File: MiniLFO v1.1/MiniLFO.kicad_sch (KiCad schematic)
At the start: 18 parts, among them U1 TL074

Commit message: Updated docs
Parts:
- removed RANGE_SW1: SW_DPDT_x2, benjiaomodular:ToggleSwitch_MTS-202_DPDT, symbol Switch:SW_DPDT_x2
- added RANGE_SW1: SW_SPDT, benjiaomodular:ToggleSwitch_MTS-102_SPDT, symbol Switch:SW_SPDT
- C1: footprint Capacitor_SMD:C_0805_2012Metric_Pad1.18x1.45mm_HandSolder -> benjiaomodular:Capacitor_Radial_D5.0mm_P2.5mm
- C2: footprint Capacitor_SMD:C_0805_2012Metric_Pad1.18x1.45mm_HandSolder -> benjiaomodular:Capacitor_Rect_L7.2mm_W2.5mm_P5.00mm
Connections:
- net TRI: now also RANGE_SW1.2 (B)
- net at C1.2: now also RANGE_SW1.1 (A)
- net at C2.2: now also RANGE_SW1.3 (C)
- net SQR: no longer names the net of R5.1, U1.7
- no-connect marks 2 -> 1
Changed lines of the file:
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@@
   (title_block
     (title "MiniLFO")
-    (rev "v1.0")
+    (rev "v1.1")
   )
   (junction (at 79.248 64.77) (diameter 0) (color 0 0 0 0)
@@
   (junction (at 146.304 59.69) (diameter 0) (color 0 0 0 0)
   )
-  (junction (at 134.874 69.85) (diameter 0) (color 0 0 0 0)
-  )
   (junction (at 81.28 49.784) (diameter 0) (color 0 0 0 0)
   )
@@
   (junction (at 74.676 123.444) (diameter 0) (color 0 0 0 0)
   )
-  (no_connect (at 307.467 75.692))
   (no_connect (at 206.248 45.72))
   (wire (pts (xy 146.304 59.69) (xy 146.304 38.1))
@@
     (stroke (width 0) (type default) (color 0 0 0 0))
   )
-  (wire (pts (xy 134.874 69.85) (xy 136.144 69.85))
+  (wire (pts (xy 133.604 69.85) (xy 136.144 69.85))
     (stroke (width 0) (type default) (color 0 0 0 0))
   )
@@
   )
   (wire (pts (xy 172.974 45.72) (xy 175.514 45.72))
-    (stroke (width 0) (type default) (color 0 0 0 0))
-  )
-  (wire (pts (xy 133.604 69.85) (xy 134.874 69.85))
-    (stroke (width 0) (type default) (color 0 0 0 0))
-  )
-  (wire (pts (xy 134.874 69.85) (xy 134.874 72.898))
     (stroke (width 0) (type default) (color 0 0 0 0))
   )
@@
     )
   )
-  (global_label "SQR" (shape output) (at 134.874 72.898 270) (fields_autoplaced)
-    (effects (font (size 1.27 1.27)) (justify right))
-    (property "Intersheet References" "${INTERSHEET_REFS}" (id 0) (at 134.7946 79.0322 90)
-      (effects (font (size 1.27 1.27)) (justify right) hide)
-    )
-  )
   (symbol (lib_id "power:GND") (at 146.304 82.55 0) (unit 1)
     (in_bom yes) (on_board yes) (fields_autoplaced)
@@
     )
     (property "Datasheet" "" (id 3) (at 146.304 82.55 0)
+      (effects (font (size 1.27 1.27)) hide)
+    )
+    (pin "1")
+  )
+  (symbol (lib_id "power:PWR_FLAG") (at 74.676 123.444 270) (unit 1)
+    (in_bom yes) (on_board yes) (fields_autoplaced)
+    (property "Reference" "#FLG0102" (id 0) (at 76.581 123.444 0)
+      (effects (font (size 1.27 1.27)) hide)
+    )
+    (property "Value" "PWR_FLAG" (id 1) (at 78.74 123.4439 90)
+      (effects (font (size 1.27 1.27)) (justify left) hide)
+    )
+    (property "Footprint" "" (id 2) (at 74.676 123.444 0)
+      (effects (font (size 1.27 1.27)) hide)
+    )
+    (property "Datasheet" "~" (id 3) (at 74.676 123.444 0)
       (effects (font (size 1.27 1.27)) hide)
     )
@@
     (pin "2")
   )
+  (symbol (lib_id "Switch:SW_SPDT") (at 97.79 49.784 0) (mirror y) (unit 1)
+    (in_bom yes) (on_board yes) (fields_autoplaced)
+    (property "Reference" "RANGE_SW1" (id 0) (at 97.79 41.91 0))
+    (property "Value" "SW_SPDT" (id 1) (at 97.79 44.45 0))
+    (property "Footprint" "benjiaomodular:ToggleSwitch_MTS-102_SPDT" (id 2) (at 97.79 49.784 0)
+      (effects (font (size 1.27 1.27)) hide)
+    )
+    (property "Datasheet" "~" (id 3) (at 97.79 49.784 0)
+      (effects (font (size 1.27 1.27)) hide)
+    )
+    (pin "1")
+    (pin "2")
+    (pin "3")
+  )
   (symbol (lib_id "Amplifier_Operational:TL074") (at 125.984 69.85 0) (unit 2)
     (in_bom yes) (on_board yes)
@@
     (property "Reference" "C1" (id 0) (at 86.614 42.164 90))
     (property "Value" "10uF" (id 1) (at 86.614 43.688 90))
-    (property "Footprint" "Capacitor_SMD:C_0805_2012Metric_Pad1.18x1.45mm_HandSolder" (id 2) (at 90.424 46.2788 0)
+    (property "Footprint" "benjiaomodular:Capacitor_Radial_D5.0mm_P2.5mm" (id 2) (at 90.424 46.2788 0)
       (effects (font (size 1.27 1.27)) hide)
     )
@@
     (pin "1")
   )
-  (symbol (lib_id "Switch:SW_DPDT_x2") (at 97.79 49.784 0) (mirror y) (unit 1)
-    (in_bom yes) (on_board yes)
-    (property "Reference" "RANGE_SW1" (id 0) (at 100.33 43.434 0))
-    (property "Value" "SW_DPDT_x2" (id 1) (at 99.695 45.339 0))
-    (property "Footprint" "benjiaomodular:ToggleSwitch_MTS-202_DPDT" (id 2) (at 97.79 49.784 0)
-      (effects (font (size 1.27 1.27)) hide)
-    )
-    (property "Datasheet" "~" (id 3) (at 97.79 49.784 0)
-      (effects (font (size 1.27 1.27)) hide)
-    )
-    (pin "1")
-    (pin "2")
-    (pin "3")
-    (pin "4")
-    (pin "5")
-    (pin "6")
-  )
   (symbol (lib_id "Device:C") (at 70.104 118.364 180) (unit 1)
     (in_bom yes) (on_board yes)
@@
     (pin "2")
   )
+  (symbol (lib_id "power:PWR_FLAG") (at 74.676 103.632 270) (unit 1)
+    (in_bom yes) (on_board yes) (fields_autoplaced)
+    (property "Reference" "#FLG0101" (id 0) (at 76.581 103.632 0)
+      (effects (font (size 1.27 1.27)) hide)
+    )
+    (property "Value" "PWR_FLAG" (id 1) (at 78.74 103.6319 90)
+      (effects (font (size 1.27 1.27)) (justify left) hide)
+    )
+    (property "Footprint" "" (id 2) (at 74.676 103.632 0)
+      (effects (font (size 1.27 1.27)) hide)
+    )
+    (property "Datasheet" "~" (id 3) (at 74.676 103.632 0)
+      (effects (font (size 1.27 1.27)) hide)
+    )
+    (pin "1")
+  )
   (symbol (lib_id "Device:C") (at 86.614 52.324 90) (unit 1)
     (in_bom yes) (on_board yes)
     (property "Reference" "C2" (id 0) (at 86.614 55.626 90))
     (property "Value" "10nF" (id 1) (at 86.614 57.15 90))
-    (property "Footprint" "Capacitor_SMD:C_0805_2012Metric_Pad1.18x1.45mm_HandSolder" (id 2) (at 90.424 51.3588 0)
+    (property "Footprint" "benjiaomodular:Capacitor_Rect_L7.2mm_W2.5mm_P5.00mm" (id 2) (at 90.424 51.3588 0)
       (effects (font (size 1.27 1.27)) hide)
     )
@@
       (reference "#FLG01") (unit 1) (value "PWR_FLAG") (footprint "")
     )
+    (path "/dd378bfc-8a6a-465f-999e-397d2de0f72e"
+      (reference "#FLG0101") (unit 1) (value "PWR_FLAG") (footprint "")
+    )
+    (path "/10d91be2-03d6-4b79-b9d6-5a488512662c"
+      (reference "#FLG0102") (unit 1) (value "PWR_FLAG") (footprint "")
+    )
     (path "/5bf9074a-d928-4bb2-baf9-82f5df81d698"
       (reference "#PWR01") (unit 1) (value "GND") (footprint "")
@@
     )
     (path "/75f8f22f-f86c-4afa-9820-4beeb807876c"
-      (reference "C1") (unit 1) (value "10uF") (footprint "Capacitor_SMD:C_0805_2012Metric_Pad1.18x1.45mm_HandSolder")
+      (reference "C1") (unit 1) (value "10uF") (footprint "benjiaomodular:Capacitor_Radial_D5.0mm_P2.5mm")
     )
     (path "/f26174fe-9829-4c03-89f7-ff8a026b9654"
-      (reference "C2") (unit 1) (value "10nF") (footprint "Capacitor_SMD:C_0805_2012Metric_Pad1.18x1.45mm_HandSolder")
+      (reference "C2") (unit 1) (value "10nF") (footprint "benjiaomodular:Capacitor_Rect_L7.2mm_W2.5mm_P5.00mm")
     )
     (path "/f2d15499-4166-4291-9f7e-40118559992b/f0c47c54-c94f-49c4-ac4e-3132ae4fcc66"
@@
       (reference "RANGE1") (unit 1) (value "B100k") (footprint "benjiaomodular:Potentiometer_RV09")
     )
-    (path "/d6bf2f45-0786-4fd9-95d1-89fd6876538f"
-      (reference "RANGE_SW1") (unit 1) (value "SW_DPDT_x2") (footprint "benjiaomodular:ToggleSwitch_MTS-202_DPDT")
+    (path "/5026acd7-845a-4552-b08c-495acad339ef"
+      (reference "RANGE_SW1") (unit 1) (value "SW_SPDT") (footprint "benjiaomodular:ToggleSwitch_MTS-102_SPDT")
     )
     (path "/5ce7ff12-274d-4130-82c4-ed37766a78af"

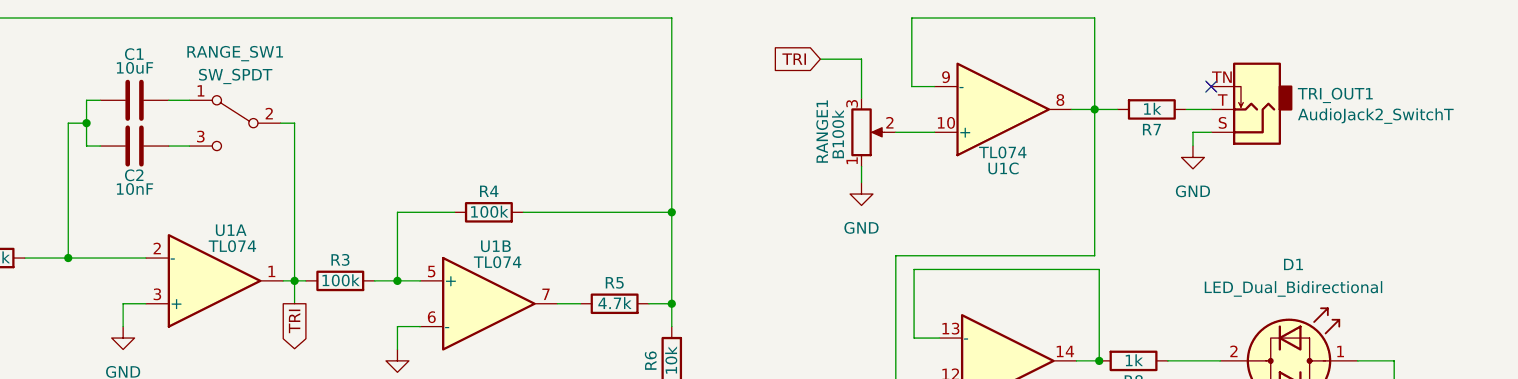
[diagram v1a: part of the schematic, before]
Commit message: Added complete bom
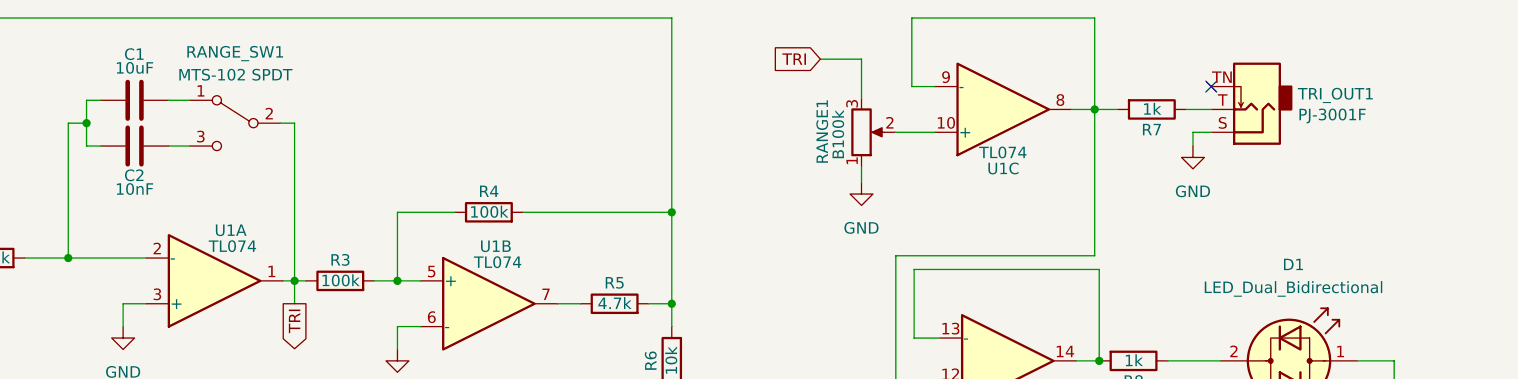
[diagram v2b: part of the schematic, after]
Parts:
- C1: Manufacturers Name (none) -> Panasonic; Manufacturers Part Number (none) -> ECE-A1VN100UB
- C2: Manufacturers Name (none) -> KEMET; Manufacturers Part Number (none) -> MMK5103K50J01L4BULK
- C4, C5: Manufacturers Name (none) -> KEMET; Manufacturers Part Number (none) -> R82EC3100DQ70K
- D1: Manufacturers Name (none) -> KENTO; Manufacturers Part Number (none) -> 3ARG4HWC
- R1: Manufacturers Name (none) -> YAGEO; Manufacturers Part Number (none) -> RC0603FR-7W470RL
- R2, R3, R4: Manufacturers Name (none) -> YAGEO; Manufacturers Part Number (none) -> RC0603FR-07100KL
- R5: Manufacturers Name (none) -> YAGEO; Manufacturers Part Number (none) -> RC0603FR-074K7L
- R6: Manufacturers Name (none) -> YAGEO; Manufacturers Part Number (none) -> AC0603FR-0710KL
- R7, R8: Manufacturers Name (none) -> YAGEO; Manufacturers Part Number (none) -> RC0603FR-071KL
- RANGE1, TIME1: Manufacturers Name (none) -> Alpha (Taiwan); Manufacturers Part Number (none) -> RV09AF-40-20K-B100K
- RANGE_SW1: value SW_SPDT -> MTS-102 SPDT; Manufacturers Name (none) -> Tayda Electronics; Manufacturers Part Number (none) -> Mini Toggle Switch SPDT On-On
- TRI_OUT1: value AudioJack2_SwitchT -> PJ-3001F
- U1: Manufacturers Name (none) -> STMicroelectronics; Manufacturers Part Number (none) -> TL074ACDT
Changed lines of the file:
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@@
+      (effects (font (size 1.27 1.27)) hide)
+    )
+    (property "Manufacturers Name" "YAGEO" (id 4) (at 109.474 67.31 0)
+      (effects (font (size 1.27 1.27)) hide)
+    )
+    (property "Manufacturers Part Number" "RC0603FR-07100KL " (id 5) (at 109.474 67.31 0)
       (effects (font (size 1.27 1.27)) hide)
     )
@@
     )
     (property "Datasheet" "http://www.ti.com/lit/ds/symlink/tl071.pdf" (id 3) (at 184.912 81.28 0)
+      (effects (font (size 1.27 1.27)) hide)
+    )
+    (property "Manufacturers Name" "STMicroelectronics" (id 4) (at 183.642 76.2 0)
+      (effects (font (size 1.27 1.27)) hide)
+    )
+    (property "Manufacturers Part Number" "TL074ACDT" (id 5) (at 183.642 76.2 0)
       (effects (font (size 1.27 1.27)) hide)
     )
@@
       (effects (font (size 1.27 1.27)) hide)
     )
+    (property "Manufacturers Name" "YAGEO" (id 4) (at 146.304 76.2 0)
+      (effects (font (size 1.27 1.27)) hide)
+    )
+    (property "Manufacturers Part Number" "AC0603FR-0710KL" (id 5) (at 146.304 76.2 0)
+      (effects (font (size 1.27 1.27)) hide)
+    )
     (pin "1")
     (pin "2")
@@
       (effects (font (size 1.27 1.27)) hide)
     )
+    (property "Manufacturers Name" "YAGEO" (id 4) (at 139.954 69.85 0)
+      (effects (font (size 1.27 1.27)) hide)
+    )
+    (property "Manufacturers Part Number" "RC0603FR-074K7L" (id 5) (at 139.954 69.85 0)
+      (effects (font (size 1.27 1.27)) hide)
+    )
     (pin "1")
     (pin "2")
@@
     )
     (property "Datasheet" "~" (id 3) (at 167.386 50.8 0)
+      (effects (font (size 1.27 1.27)) hide)
+    )
+    (property "Manufacturers Name" "Alpha (Taiwan)" (id 4) (at 167.386 50.8 0)
+      (effects (font (size 1.27 1.27)) hide)
+    )
+    (property "Manufacturers Part Number" "RV09AF-40-20K-B100K" (id 5) (at 167.386 50.8 0)
       (effects (font (size 1.27 1.27)) hide)
     )
@@
       (effects (font (size 1.27 1.27)) hide)
     )
+    (property "Manufacturers Name" "YAGEO" (id 4) (at 125.984 59.69 0)
+      (effects (font (size 1.27 1.27)) hide)
+    )
+    (property "Manufacturers Part Number" "RC0603FR-07100KL " (id 5) (at 125.984 59.69 0)
+      (effects (font (size 1.27 1.27)) hide)
+    )
     (pin "1")
     (pin "2")
@@
     (in_bom yes) (on_board yes) (fields_autoplaced)
     (property "Reference" "RANGE_SW1" (id 0) (at 97.79 41.91 0))
-    (property "Value" "SW_SPDT" (id 1) (at 97.79 44.45 0))
+    (property "Value" "MTS-102 SPDT" (id 1) (at 97.79 44.45 0))
     (property "Footprint" "benjiaomodular:ToggleSwitch_MTS-102_SPDT" (id 2) (at 97.79 49.784 0)
       (effects (font (size 1.27 1.27)) hide)
     )
     (property "Datasheet" "~" (id 3) (at 97.79 49.784 0)
+      (effects (font (size 1.27 1.27)) hide)
+    )
+    (property "Manufacturers Name" "Tayda Electronics" (id 4) (at 97.79 49.784 0)
+      (effects (font (size 1.27 1.27)) hide)
+    )
+    (property "Manufacturers Part Number" "Mini Toggle Switch SPDT On-On" (id 5) (at 97.79 49.784 0)
       (effects (font (size 1.27 1.27)) hide)
     )
@@
     )
     (property "Datasheet" "http://www.ti.com/lit/ds/symlink/tl071.pdf" (id 3) (at 127.254 64.77 0)
+      (effects (font (size 1.27 1.27)) hide)
+    )
+    (property "Manufacturers Name" "STMicroelectronics" (id 4) (at 125.984 69.85 0)
+      (effects (font (size 1.27 1.27)) hide)
+    )
+    (property "Manufacturers Part Number" "TL074ACDT" (id 5) (at 125.984 69.85 0)
       (effects (font (size 1.27 1.27)) hide)
     )
@@
       (effects (font (size 1.27 1.27)) hide)
     )
+    (property "Manufacturers Name" "KEMET" (id 4) (at 70.104 108.712 0)
+      (effects (font (size 1.27 1.27)) hide)
+    )
+    (property "Manufacturers Part Number" "R82EC3100DQ70K " (id 5) (at 70.104 108.712 0)
+      (effects (font (size 1.27 1.27)) hide)
+    )
     (pin "1")
     (pin "2")
@@
     )
     (property "Datasheet" "~" (id 3) (at 60.96 64.77 0)
+      (effects (font (size 1.27 1.27)) hide)
+    )
+    (property "Manufacturers Name" "Alpha (Taiwan)" (id 4) (at 60.96 64.77 0)
+      (effects (font (size 1.27 1.27)) hide)
+    )
+    (property "Manufacturers Part Number" "RV09AF-40-20K-B100K" (id 5) (at 60.96 64.77 0)
       (effects (font (size 1.27 1.27)) hide)
     )
@@
       (effects (font (size 1.27 1.27)) hide)
     )
+    (property "Manufacturers Name" "YAGEO" (id 4) (at 60.96 74.93 0)
+      (effects (font (size 1.27 1.27)) hide)
+    )
+    (property "Manufacturers Part Number" "RC0603FR-7W470RL" (id 5) (at 60.96 74.93 0)
+      (effects (font (size 1.27 1.27)) hide)
+    )
     (pin "1")
     (pin "2")
@@
       (effects (font (size 1.27 1.27)) hide)
     )
+    (property "Manufacturers Name" " Panasonic" (id 4) (at 86.614 47.244 0)
+      (effects (font (size 1.27 1.27)) hide)
+    )
+    (property "Manufacturers Part Number" "ECE-A1VN100UB" (id 5) (at 86.614 47.244 0)
+      (effects (font (size 1.27 1.27)) hide)
+    )
     (pin "1")
     (pin "2")
@@
       (effects (font (size 1.27 1.27)) hide)
     )
+    (property "Manufacturers Name" "YAGEO" (id 4) (at 70.612 64.77 0)
+      (effects (font (size 1.27 1.27)) hide)
+    )
+    (property "Manufacturers Part Number" "RC0603FR-07100KL " (id 5) (at 70.612 64.77 0)
+      (effects (font (size 1.27 1.27)) hide)
+    )
     (pin "1")
     (pin "2")
@@
     )
     (property "Datasheet" "http://www.ti.com/lit/ds/symlink/tl071.pdf" (id 3) (at 184.404 53.34 0)
+      (effects (font (size 1.27 1.27)) hide)
+    )
+    (property "Manufacturers Name" "STMicroelectronics" (id 4) (at 183.134 48.26 0)
+      (effects (font (size 1.27 1.27)) hide)
+    )
+    (property "Manufacturers Part Number" "TL074ACDT" (id 5) (at 183.134 48.26 0)
       (effects (font (size 1.27 1.27)) hide)
     )
@@
       (effects (font (size 1.27 1.27)) hide)
     )
+    (property "Manufacturers Name" "STMicroelectronics" (id 4) (at 77.216 113.284 0)
+      (effects (font (size 1.27 1.27)) hide)
+    )
+    (property "Manufacturers Part Number" "TL074ACDT" (id 5) (at 77.216 113.284 0)
+      (effects (font (size 1.27 1.27)) hide)
+    )
     (pin "1")
     (pin "2")
@@
       (effects (font (size 1.27 1.27)) hide)
     )
+    (property "Manufacturers Name" "YAGEO" (id 4) (at 199.644 48.26 0)
+      (effects (font (size 1.27 1.27)) hide)
+    )
+    (property "Manufacturers Part Number" "RC0603FR-071KL " (id 5) (at 199.644 48.26 0)
+      (effects (font (size 1.27 1.27)) hide)
+    )
     (pin "1")
     (pin "2")
@@
       (effects (font (size 1.27 1.27)) hide)
     )
+    (property "Manufacturers Name" "YAGEO" (id 4) (at 197.612 76.2 0)
+      (effects (font (size 1.27 1.27)) hide)
+    )
+    (property "Manufacturers Part Number" "RC0603FR-071KL " (id 5) (at 197.612 76.2 0)
+      (effects (font (size 1.27 1.27)) hide)
+    )
     (pin "1")
     (pin "2")
@@
     )
     (property "Datasheet" "http://www.ti.com/lit/ds/symlink/tl071.pdf" (id 3) (at 96.774 72.39 0)
+      (effects (font (size 1.27 1.27)) hide)
+    )
+    (property "Manufacturers Name" "STMicroelectronics" (id 4) (at 95.504 67.31 0)
+      (effects (font (size 1.27 1.27)) hide)
+    )
+    (property "Manufacturers Part Number" "TL074ACDT" (id 5) (at 95.504 67.31 0)
       (effects (font (size 1.27 1.27)) hide)
     )
@@
       (effects (font (size 1.27 1.27)) hide)
     )
+    (property "Manufacturers Name" "KENTO" (id 4) (at 214.884 76.2 0)
+      (effects (font (size 1.27 1.27)) hide)
+    )
+    (property "Manufacturers Part Number" "3ARG4HWC" (id 5) (at 214.884 76.2 0)
+      (effects (font (size 1.27 1.27)) hide)
+    )
     (pin "1")
     (pin "2")
@@
       (effects (font (size 1.27 1.27)) (justify right))
     )
-    (property "Value" "AudioJack2_SwitchT" (id 1) (at 215.8746 48.8696 0)
+    (property "Value" "PJ-3001F" (id 1) (at 215.8746 48.8696 0)
       (effects (font (size 1.27 1.27)) (justify right))
     )
@@
       (effects (font (size 1.27 1.27)) hide)
     )
+    (property "Manufacturers Name" "KEMET" (id 4) (at 70.104 118.364 0)
+      (effects (font (size 1.27 1.27)) hide)
+    )
+    (property "Manufacturers Part Number" "R82EC3100DQ70K " (id 5) (at 70.104 118.364 0)
+      (effects (font (size 1.27 1.27)) hide)
+    )
     (pin "1")
     (pin "2")
@@
     )
     (property "Datasheet" "~" (id 3) (at 86.614 52.324 0)
+      (effects (font (size 1.27 1.27)) hide)
+    )
+    (property "Manufacturers Name" "KEMET" (id 4) (at 86.614 52.324 0)
+      (effects (font (size 1.27 1.27)) hide)
+    )
+    (property "Manufacturers Part Number" "MMK5103K50J01L4BULK" (id 5) (at 86.614 52.324 0)
       (effects (font (size 1.27 1.27)) hide)
     )
@@
     )
     (path "/5026acd7-845a-4552-b08c-495acad339ef"
-      (reference "RANGE_SW1") (unit 1) (value "SW_SPDT") (footprint "benjiaomodular:ToggleSwitch_MTS-102_SPDT")
+      (reference "RANGE_SW1") (unit 1) (value "MTS-102 SPDT") (footprint "benjiaomodular:ToggleSwitch_MTS-102_SPDT")
     )
     (path "/5ce7ff12-274d-4130-82c4-ed37766a78af"
@@
     )
     (path "/b3c1f37c-a803-4d82-81ff-b77950a51ba3"
-      (reference "TRI_OUT1") (unit 1) (value "AudioJack2_SwitchT") (footprint "benjiaomodular:AudioJack_3.5mm")
+      (reference "TRI_OUT1") (unit 1) (value "PJ-3001F") (footprint "benjiaomodular:AudioJack_3.5mm")
     )
     (path "/a85f6634-8225-4514-a272-b41bb171760d"
